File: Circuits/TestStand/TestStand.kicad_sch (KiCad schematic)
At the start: 48 parts, among them J1 Screw_Terminal_01x07, J2 Screw_Terminal_01x07, J3 Screw_Terminal_01x07, J4 Screw_Terminal_01x03, J5 Screw_Terminal_01x03, J6 Screw_Terminal_01x03, J7 Screw_Terminal_01x03, J8 Screw_Terminal_01x03, Q1 MMBT4403-7-F, Q2 MMBT4403-7-F, Q3 MMBT4403-7-F, U1 HX711, U2 HX711, U3 HX711, U4 Teensy4.1

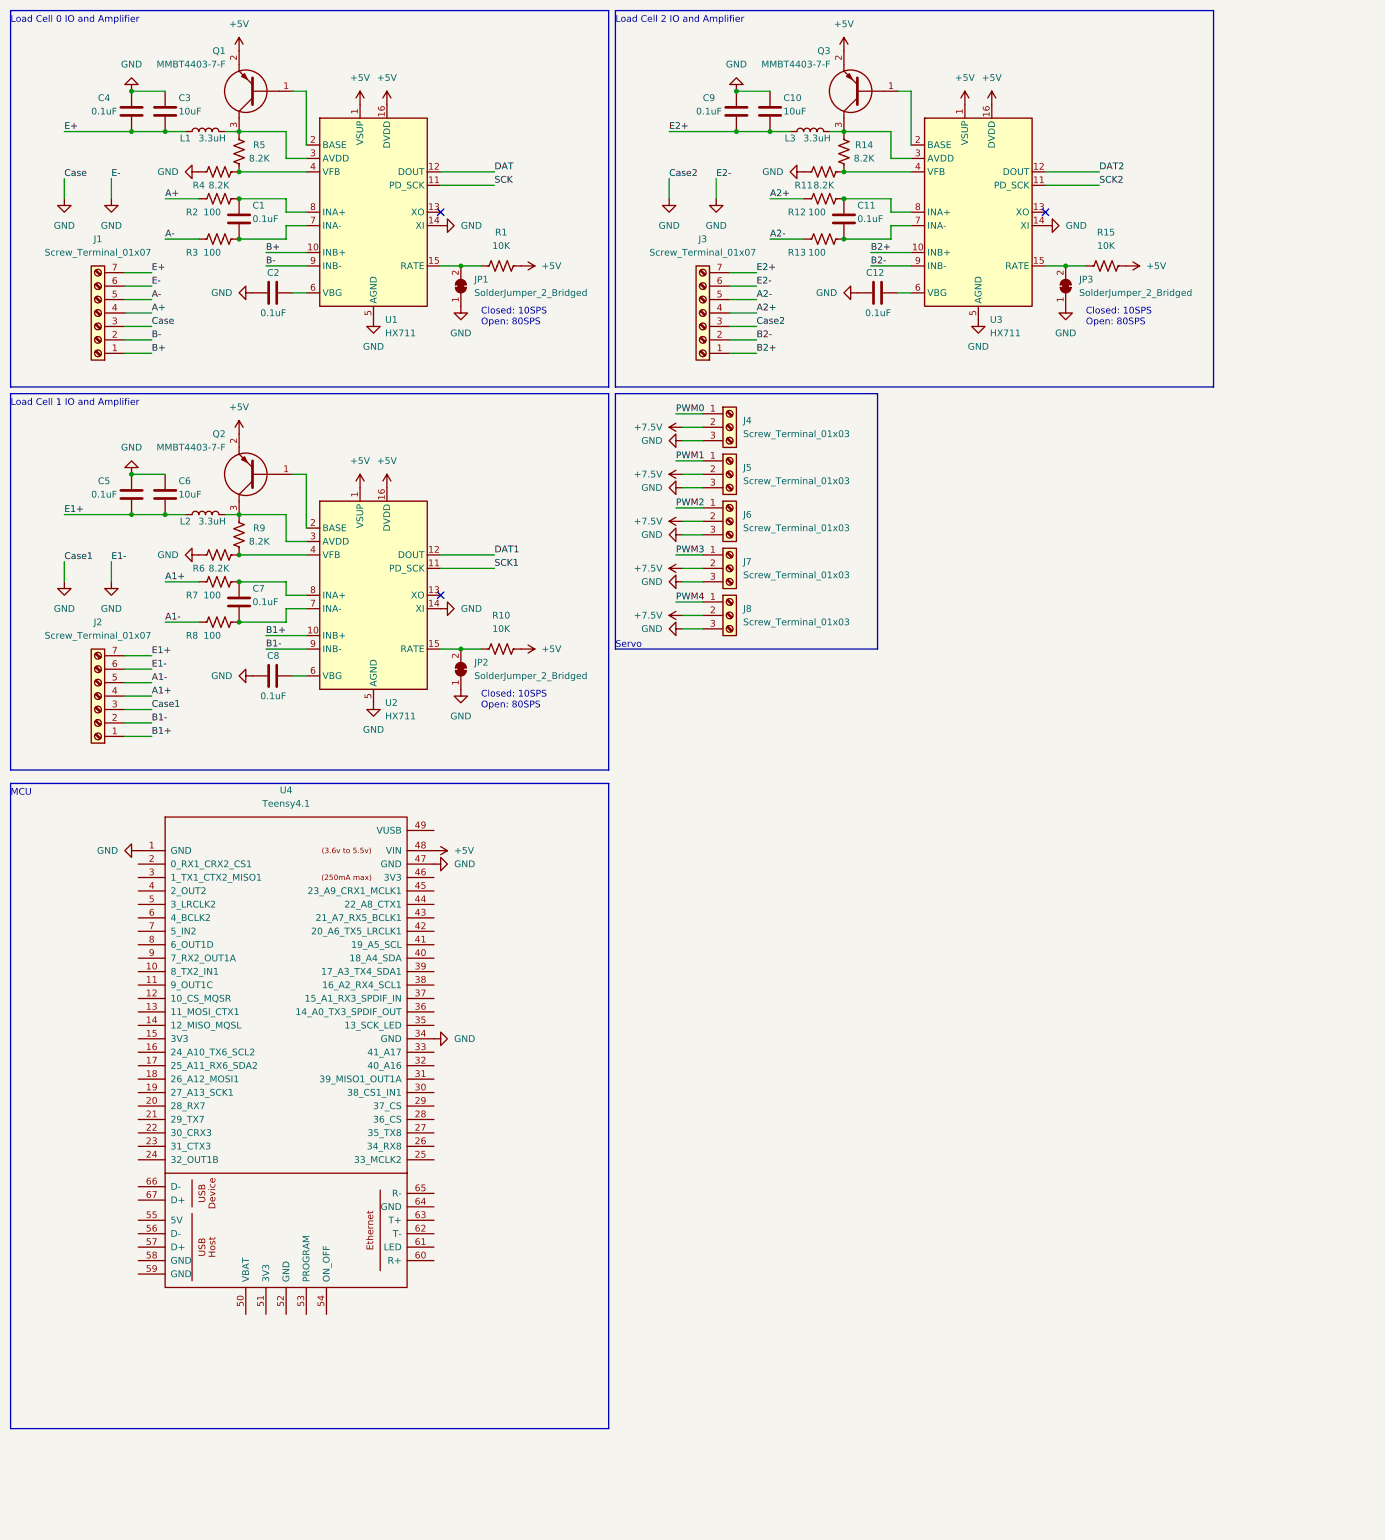
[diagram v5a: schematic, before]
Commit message: Connected servo, pts, and load cells to mcu
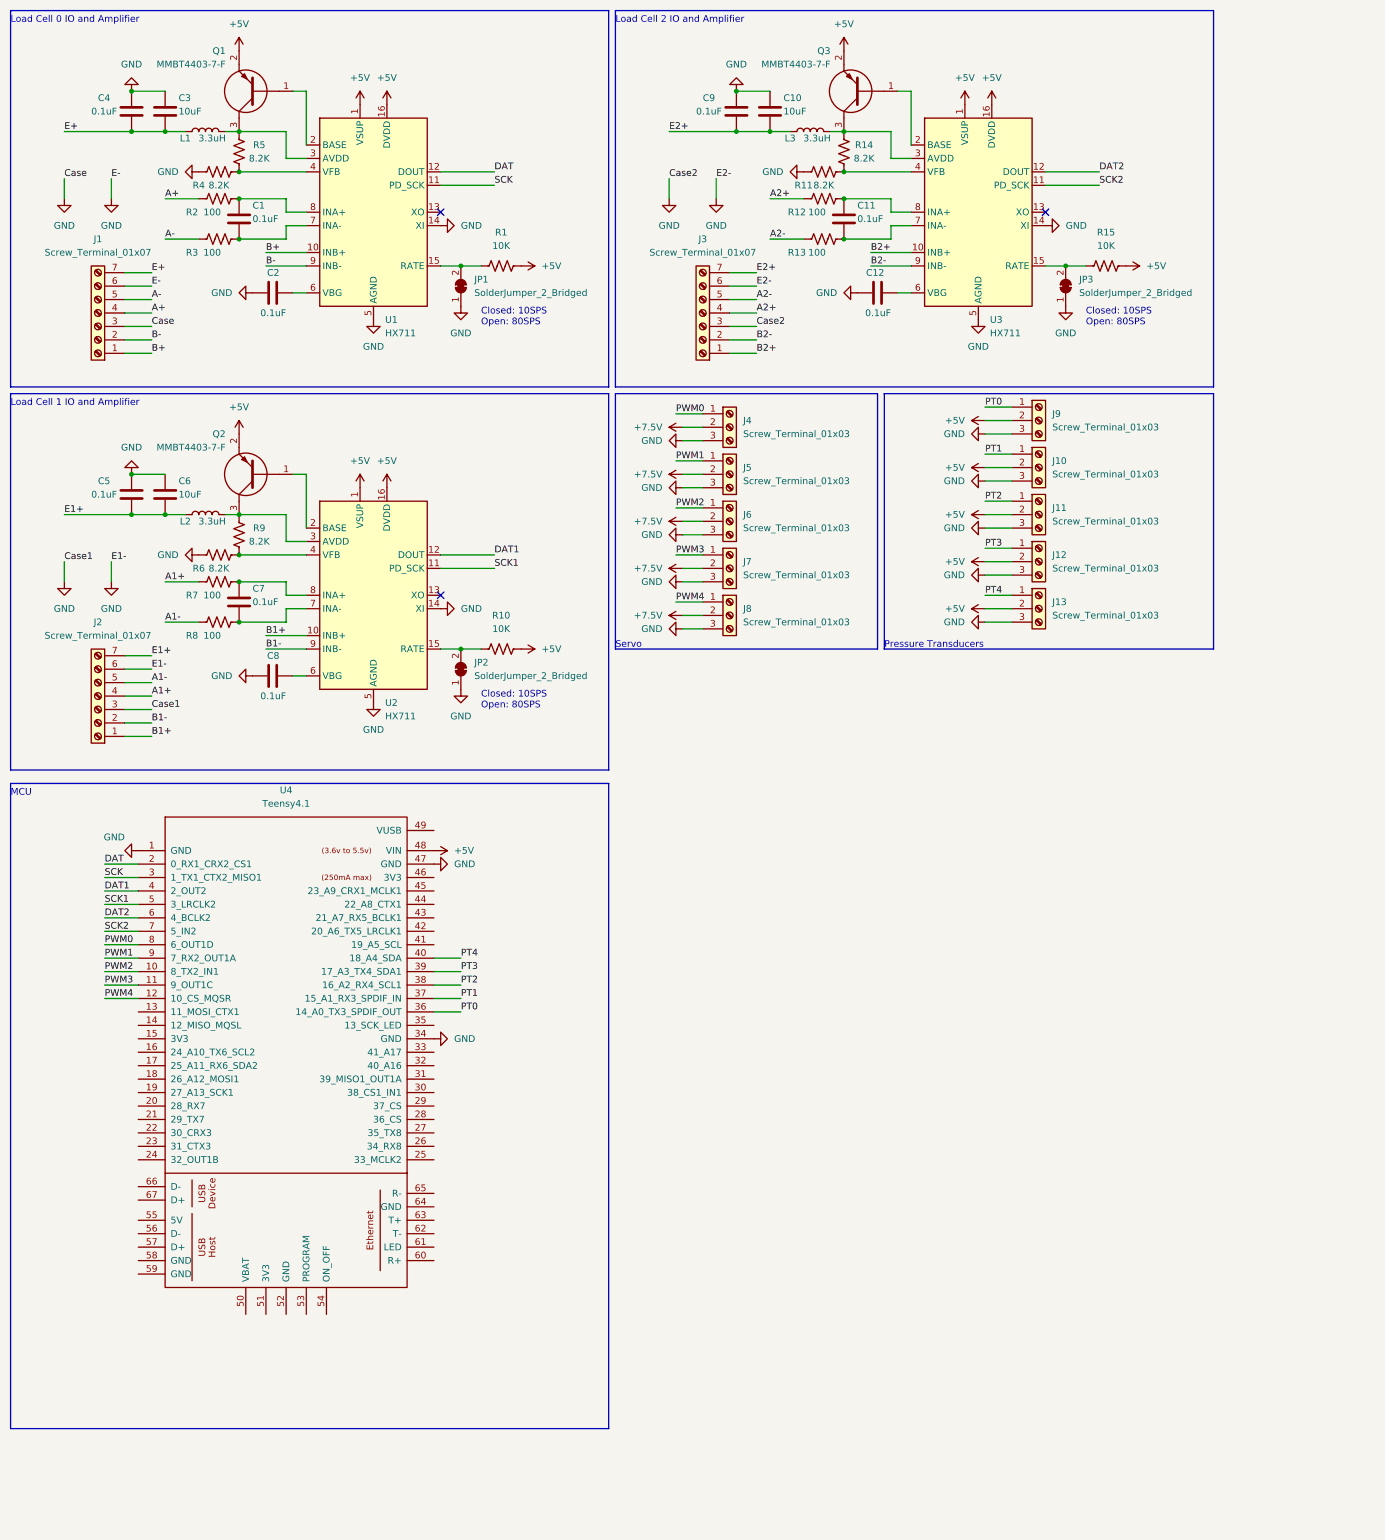
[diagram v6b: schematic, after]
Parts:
- added J10, J11, J12, J13, J9: Screw_Terminal_01x03, symbol Connector:Screw_Terminal_01x03
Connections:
- net +5V: now also J10.2 (Pin_2), J11.2 (Pin_2), J12.2 (Pin_2), J13.2 (Pin_2), J9.2 (Pin_2)
- net DAT: now also U4.2 (0_RX1_CRX2_CS1)
- net DAT1: now also U4.4 (2_OUT2)
- net DAT2: now also U4.6 (4_BCLK2)
- net GND: now also J10.3 (Pin_3), J11.3 (Pin_3), J12.3 (Pin_3), J13.3 (Pin_3), J9.3 (Pin_3)
- net PWM0: now also U4.8 (6_OUT1D)
- net PWM1: now also U4.9 (7_RX2_OUT1A)
- net PWM2: now also U4.10 (8_TX2_IN1)
- net PWM3: now also U4.11 (9_OUT1C)
- net PWM4: now also U4.12 (10_CS_MQSR)
- net SCK: now also U4.3 (1_TX1_CTX2_MISO1)
- net SCK1: now also U4.5 (3_LRCLK2)
- net SCK2: now also U4.7 (5_IN2)
- net PT0: now reaches U4.36 (14_A0_TX3_SPDIF_OUT)
- net PT0: now also J9.1 (Pin_1)
- net PT1: now reaches U4.37 (15_A1_RX3_SPDIF_IN)
- net PT1: now also J10.1 (Pin_1)
- net PT2: now reaches U4.38 (16_A2_RX4_SCL1)
- net PT2: now also J11.1 (Pin_1)
- net PT3: now reaches U4.39 (17_A3_TX4_SDA1)
- net PT3: now also J12.1 (Pin_1)
- net PT4: now reaches U4.40 (18_A4_SDA)
- net PT4: now also J13.1 (Pin_1)
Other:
- note added: "Pressure Transducers"

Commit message: Started designing the PCB
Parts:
- C1, C10, C11, C12, C2, C3, C4, C5, C6, C7, C8, C9: footprint (none) -> Capacitor_SMD:C_0805_2012Metric
- J1, J2, J3: footprint (none) -> Connector_Wago:Wago_734-137_1x07_P3.50mm_Vertical
- J10, J11, J12, J13, J4, J5, J6, J7, J8, J9: footprint (none) -> Connector_Wago:Wago_734-133_1x03_P3.50mm_Vertical
- JP1, JP2, JP3: footprint (none) -> Jumper:SolderJumper-2_P1.3mm_Bridged_RoundedPad1.0x1.5mm
- L1, L2, L3: footprint (none) -> Inductor_SMD:L_0805_2012Metric
- Q1, Q2, Q3: footprint SOT96P240X110-3N -> Library:SOT96P240X110-3N
- R1, R10, R11, R12, R13, R14, R15, R2, R3, R4, R5, R6, R7, R8, R9: footprint (none) -> Resistor_SMD:R_0805_2012Metric
- U4: footprint (none) -> Library:Teensy41

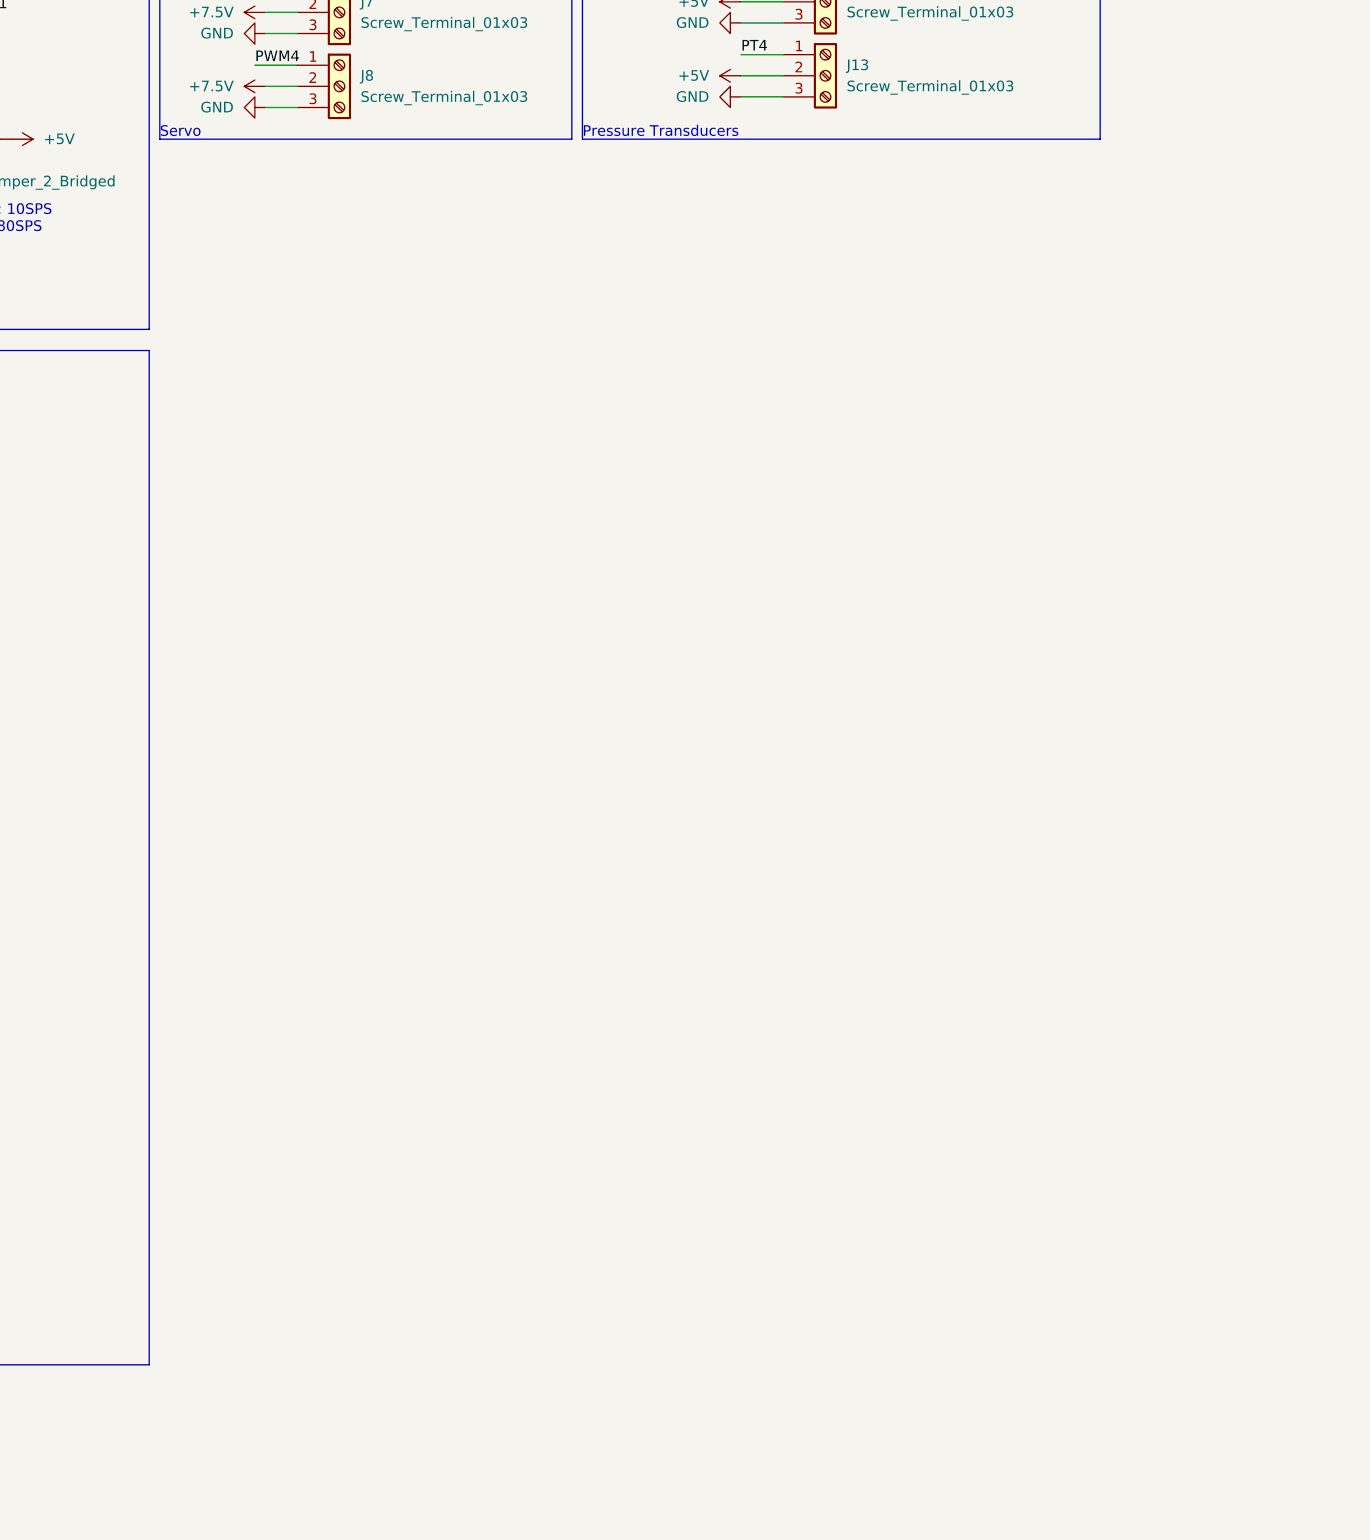
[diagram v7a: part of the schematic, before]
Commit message: Added TC and RF circuits
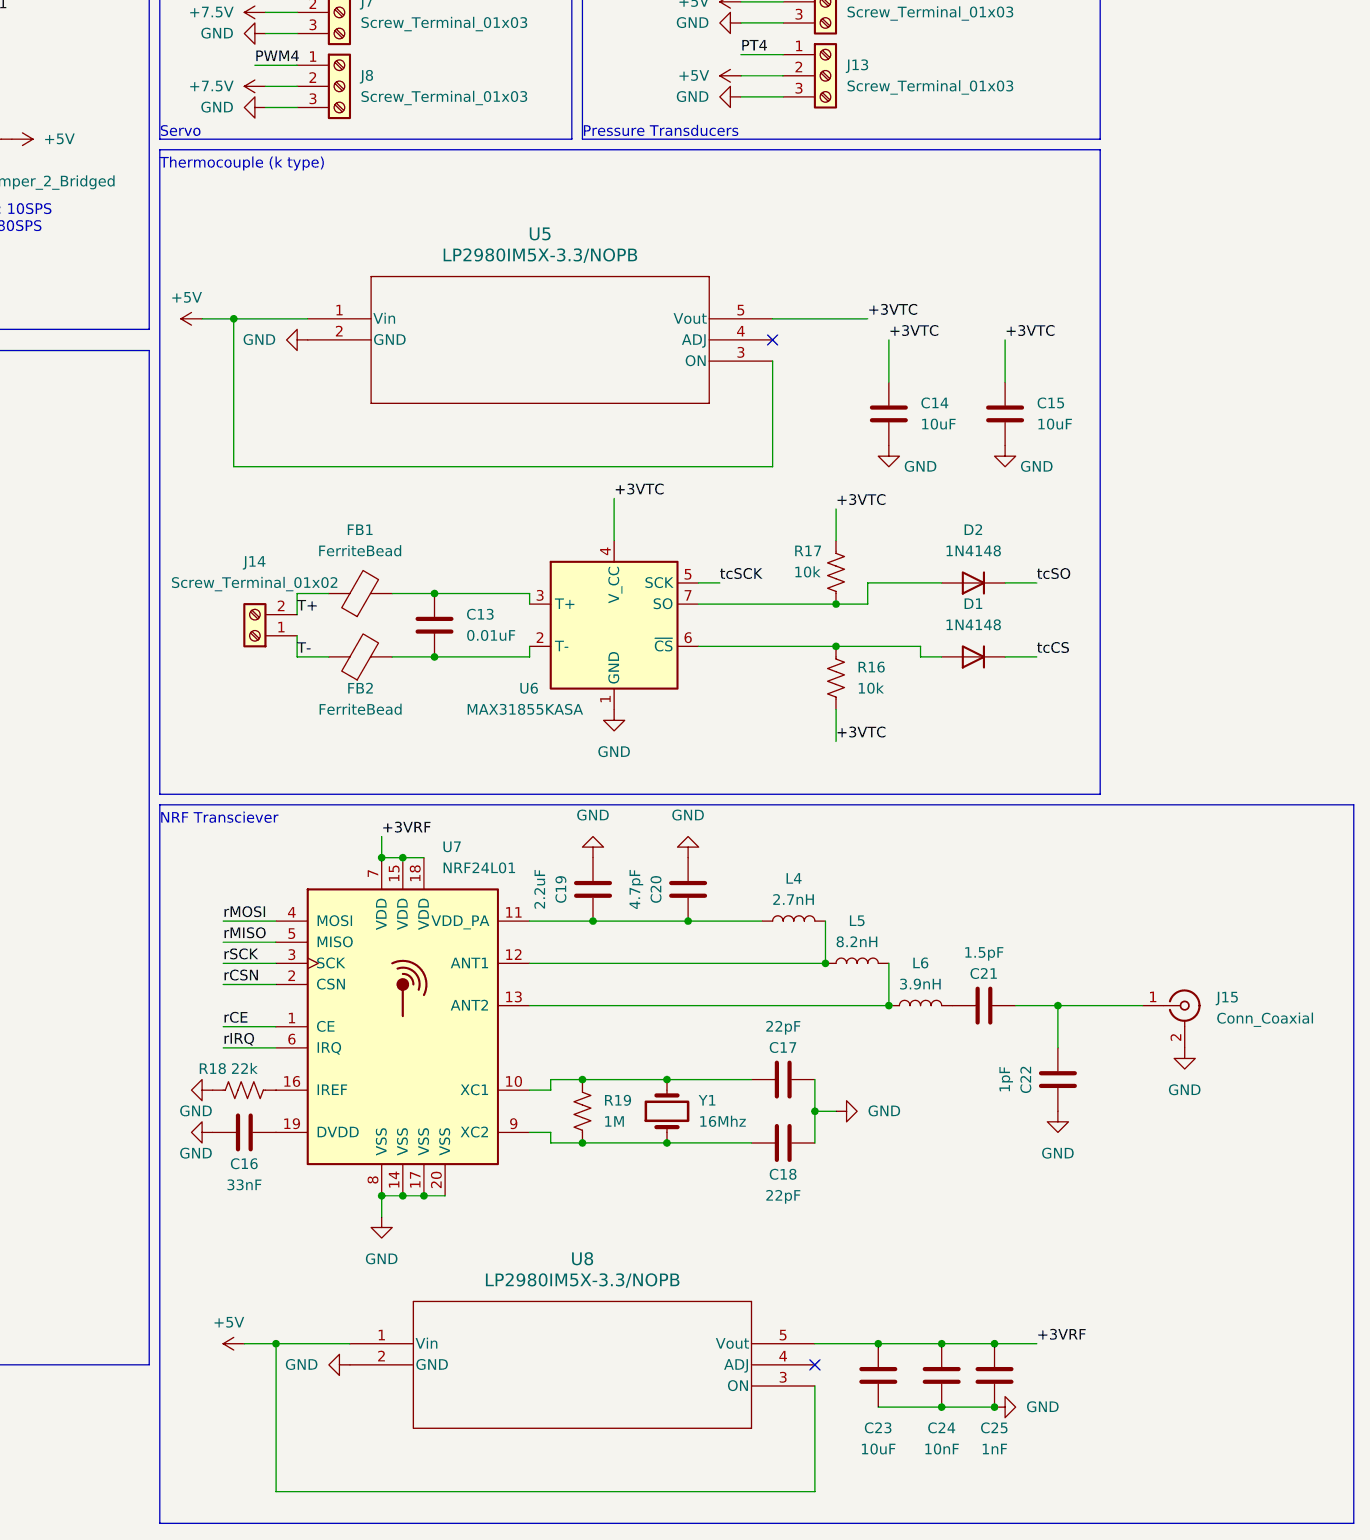
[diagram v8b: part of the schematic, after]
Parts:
- added C13: 0.01uF, symbol Device:C
- added C14, C15, C23: 10uF, symbol Device:C
- added C16: 33nF, symbol Device:C
- added C17, C18: 22pF, symbol Device:C
- added C19: 2.2uF, symbol Device:C
- added C20: 4.7pF, symbol Device:C
- added C21: 1.5pF, symbol Device:C
- added C22: 1pF, symbol Device:C
- added C24: 10nF, symbol Device:C
- added C25: 1nF, symbol Device:C
- added D1, D2: 1N4148, Diode_THT:D_DO-35_SOD27_P7.62mm_Horizontal, symbol Diode:1N4148
- added FB1, FB2: FerriteBead, symbol Device:FerriteBead
- added J14: Screw_Terminal_01x02, symbol Connector:Screw_Terminal_01x02
- added J15: Conn_Coaxial, symbol Connector:Conn_Coaxial
- added L4: 2.7nH, symbol Device:L
- added L5: 8.2nH, symbol Device:L
- added L6: 3.9nH, symbol Device:L
- added R16, R17: 10k, symbol Device:R_US
- added R18: 22k, symbol Device:R_US
- added R19: 1M, symbol Device:R_US
- added U5, U8: LP2980IM5X-3.3/NOPB, MF05A_TEX, symbol 2024-08-13_18-22-47:LP2980IM5X-3.3_NOPB
- added U6: MAX31855KASA, Package_SO:SOIC-8_3.9x4.9mm_P1.27mm, symbol Sensor_Temperature:MAX31855KASA
- added U7: NRF24L01, Package_DFN_QFN:QFN-20-1EP_4x4mm_P0.5mm_EP2.5x2.5mm, symbol RF:NRF24L01
- added Y1: 16Mhz, symbol Device:Crystal
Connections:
- net +5V: now also U5.1 (Vin), U5.3 (ON), U8.1 (Vin), U8.3 (ON)
- net GND: now also C14.2, C15.2, C16.1, C17.2, C18.2, C19.2, C20.2, C22.1, C23.1, C24.1, C25.1, J15.2 (Ext), R18.1, U5.2 (GND), U6.1 (GND), U7.14 (VSS), U7.17 (VSS), U7.20 (VSS), U7.8 (VSS), U8.2 (GND)
- new net: C21.2, C22.2, J15.1 (In)
- new net: C13.1, FB1.2, U6.3 (T+)
- new net: C13.2, FB2.2, U6.2 (T-)
- new net: C17.1, R19.1, U7.10 (XC1), Y1.2
- new net: R18.2, U7.16 (IREF)
- new net: C19.1, C20.1, L4.1, U7.11 (VDD_PA)
- new net: D1.2 (A), R16.1, U6.6 (~{CS})
- new net: D2.2 (A), R17.2, U6.7 (SO)
- new net: L4.2, L5.1, U7.12 (ANT1)
- new net: L5.2, L6.1, U7.13 (ANT2)
- new net: C18.1, R19.2, U7.9 (XC2), Y1.1
- new net: C16.2, U7.19 (DVDD)
- new net: C21.1, L6.2
- new net +3VRF: C23.2, C24.2, C25.2, U7.15 (VDD), U7.18 (VDD), U7.7 (VDD), U8.5 (Vout)
- new net +3VTC: C14.1, C15.1, R16.2, R17.1, U5.5 (Vout), U6.4 (V_CC)
- new net T+: FB1.1, J14.2 (Pin_2)
- new net T-: FB2.1, J14.1 (Pin_1)
- new net rCE: U7.1 (CE)
- new net rCSN: U7.2 (CSN)
- new net rIRQ: U7.6 (IRQ)
- new net rMISO: U7.5 (MISO)
- new net rMOSI: U7.4 (MOSI)
- new net rSCK: U7.3 (SCK)
- new net tcCS: D1.1 (K)
- new net tcSCK: U6.5 (SCK)
- new net tcSO: D2.1 (K)
- no-connect marks 3 -> 5
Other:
- note added: "NRF Transciever"
- note added: "Thermocouple (k type)"
